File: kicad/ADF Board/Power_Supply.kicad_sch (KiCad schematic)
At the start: 21 parts, among them U401 AMS1117-3.3

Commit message: Finished board, DRC OK, silkscreen done, sheets versioned. Ready for export.
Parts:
- added TP321: 5V_between-fuse-and-ferrite, TestPoint:TestPoint_Pad_D1.0mm, symbol Connector:TestPoint_Small
- renumbered C407 to C201, C406 to C202, C405 to C203, C157 to C204, C403 to C205, C402 to C206, C161 to C207, C404 to C208, C401 to C209, C151 to C210, C408 to C211, C153 to C212, C409 to C213, D19 to D201, D401 to D202, D12 to D203, F401 to F201, FB3 to FB201, TP30 to TP201, TP27 to TP202, U401 to U201
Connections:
- net at C201.1, C202.2, C203.1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: now also TP321.1
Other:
- company: (none) -> openUC2 GmbH
- title: (none) -> QuantumMiniLabs_ODMR::ADF_Board

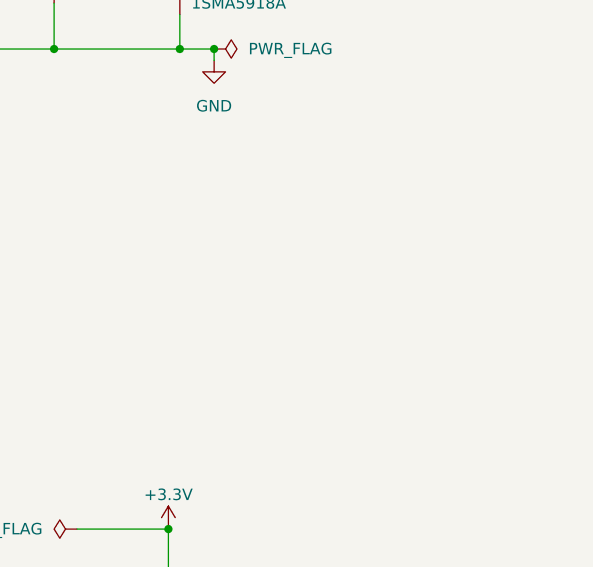
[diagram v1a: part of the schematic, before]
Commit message: Rev. B: Added a big GND testpoint and fixed minor silkscreen label inaccuracies
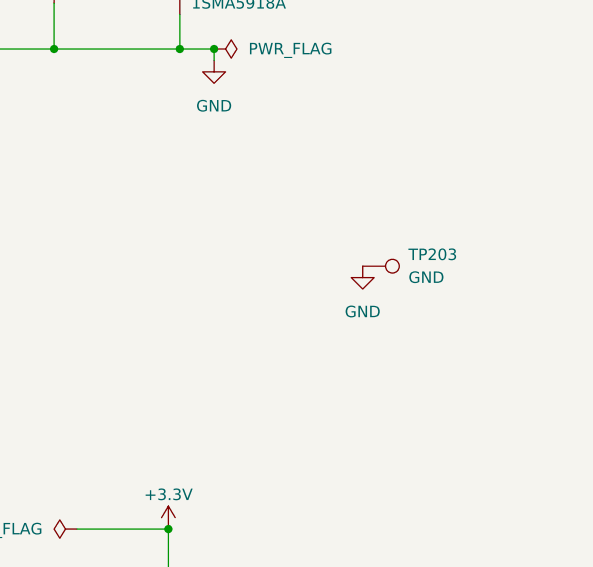
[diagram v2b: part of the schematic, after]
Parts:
- added TP203: GND, TestPoint:TestPoint_Pad_D2.0mm, symbol Connector:TestPoint
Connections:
- net GND: now also TP203.1
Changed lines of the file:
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@@
 	(title_block
 		(title "QuantumMiniLabs_ODMR::ADF_Board")
-		(date "2025-03-01")
-		(rev "A")
+		(date "2025-12-08")
+		(rev "B")
 		(company "openUC2 GmbH")
 		(comment 1 "christiankuttke based on design by Dennis Stiegekötter")
@@
 	)
 	(symbol
+		(lib_id "Connector:TestPoint")
+		(at 182.88 90.17 270)
+		(unit 1)
+		(exclude_from_sim no)
+		(in_bom yes)
+		(on_board yes)
+		(dnp no)
+		(fields_autoplaced yes)
+		(property "Reference" "TP203"
+			(at 187.96 88.8999 90)
+			(effects
+				(font
+					(size 1.27 1.27)
+				)
+				(justify left)
+			)
+		)
+		(property "Value" "GND"
+			(at 187.96 91.4399 90)
+			(effects
+				(font
+					(size 1.27 1.27)
+				)
+				(justify left)
+			)
+		)
+		(property "Footprint" "TestPoint:TestPoint_Pad_D2.0mm"
+			(at 182.88 95.25 0)
+			(effects
+				(font
+					(size 1.27 1.27)
+				)
+				(hide yes)
+			)
+		)
+		(property "Datasheet" "~"
+			(at 182.88 95.25 0)
+			(effects
+				(font
+					(size 1.27 1.27)
+				)
+				(hide yes)
+			)
+		)
+		(property "Description" ""
+			(at 182.88 90.17 0)
+			(effects
+				(font
+					(size 1.27 1.27)
+				)
+				(hide yes)
+			)
+		)
+		(property "Description_1" ""
+			(at 182.88 90.17 0)
+			(effects
+				(font
+					(size 1.27 1.27)
+				)
+				(hide yes)
+			)
+		)
+		(pin "1"
+		)
+		(instances
+			(project "ADF_Board"
+				(path "/90b3de2f-c818-48df-8078-fde6a4536a1f/231aed12-61f6-4ebe-919d-1b056d963af2"
+					(reference "TP203")
+					(unit 1)
+				)
+			)
+		)
+	)
+	(symbol
 		(lib_id "Device:C_Small")
 		(at 85.09 48.26 0)
@@
 					(unit 1)
 				)
+			)
+		)
+	)
+	(symbol
+		(lib_name "GND_1")
+		(lib_id "power:GND")
+		(at 182.88 90.17 0)
+		(unit 1)
+		(exclude_from_sim no)
+		(in_bom yes)
+		(on_board yes)
+		(dnp no)
+		(fields_autoplaced yes)
+		(property "Reference" "#PWR0211"
+			(at 182.88 96.52 0)
+			(effects
+				(font
+					(size 1.27 1.27)
+				)
+				(hide yes)
+			)
+		)
+		(property "Value" "GND"
+			(at 182.88 95.25 0)
+			(effects
+				(font
+					(size 1.27 1.27)
+				)
+			)
+		)
+		(property "Footprint" ""
+			(at 182.88 90.17 0)
+			(effects
+				(font
+					(size 1.27 1.27)
+				)
+				(hide yes)
+			)
+		)
+		(property "Datasheet" ""
+			(at 182.88 90.17 0)
+			(effects
+				(font
+					(size 1.27 1.27)
+				)
+				(hide yes)
+			)
+		)
+		(property "Description" "Power symbol creates a global label with name \"GND\" , ground"
+			(at 182.88 90.17 0)
+			(effects
+				(font
+					(size 1.27 1.27)
+				)
+				(hide yes)
+			)
+		)
+		(pin "1"
+		)
+		(instances
+			(project ""
+				(path "/90b3de2f-c818-48df-8078-fde6a4536a1f/231aed12-61f6-4ebe-919d-1b056d963af2"
+					(reference "#PWR0211")
+					(unit 1)
+				)
